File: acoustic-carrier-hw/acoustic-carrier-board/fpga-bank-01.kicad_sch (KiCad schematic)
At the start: 11 parts, among them IC1 ECP5-BGA256, Y401 Crystal Oscillator

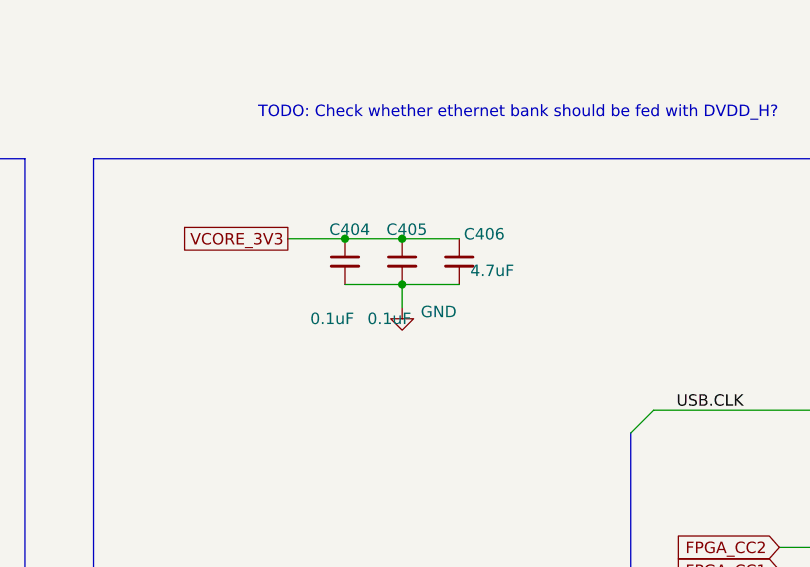
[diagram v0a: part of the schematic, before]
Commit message: [carrier] Added 2 buttons and 2 leds + routing
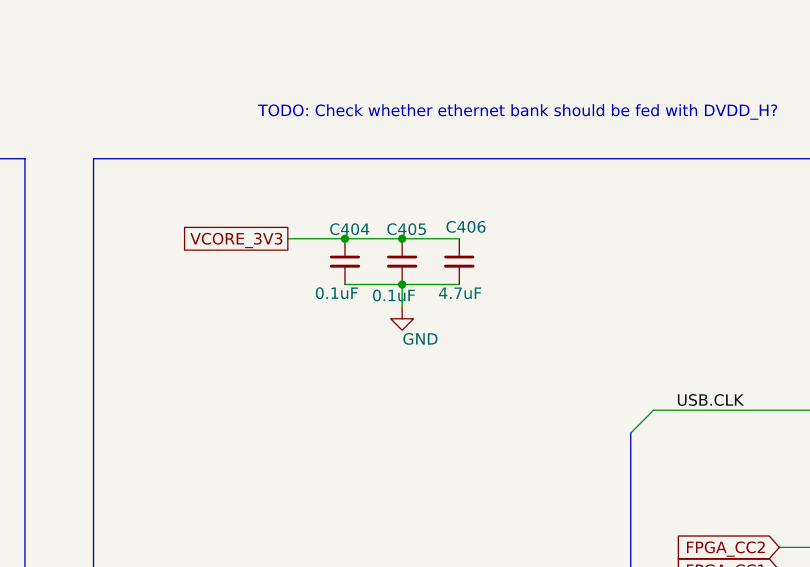
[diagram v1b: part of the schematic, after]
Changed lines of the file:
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@@
 		(dnp no)
 		(property "Reference" "C406"
-			(at 197.358 45.212 0)
+			(at 195.326 44.45 0)
 			(effects
 				(font
@@
 		)
 		(property "Value" "4.7uF"
-			(at 202.946 49.276 0)
+			(at 199.39 51.816 0)
 			(effects
 				(font
@@
 		)
 		(property "Value" "GND"
-			(at 194.564 53.848 0)
+			(at 192.532 56.896 0)
 			(effects
 				(font
@@
 		)
 		(property "Value" "0.1uF"
-			(at 185.166 54.61 0)
+			(at 185.674 51.816 0)
 			(effects
 				(font
@@
 		)
 		(property "Value" "0.1uF"
-			(at 191.516 54.61 0)
+			(at 192.024 52.07 0)
 			(effects
 				(font

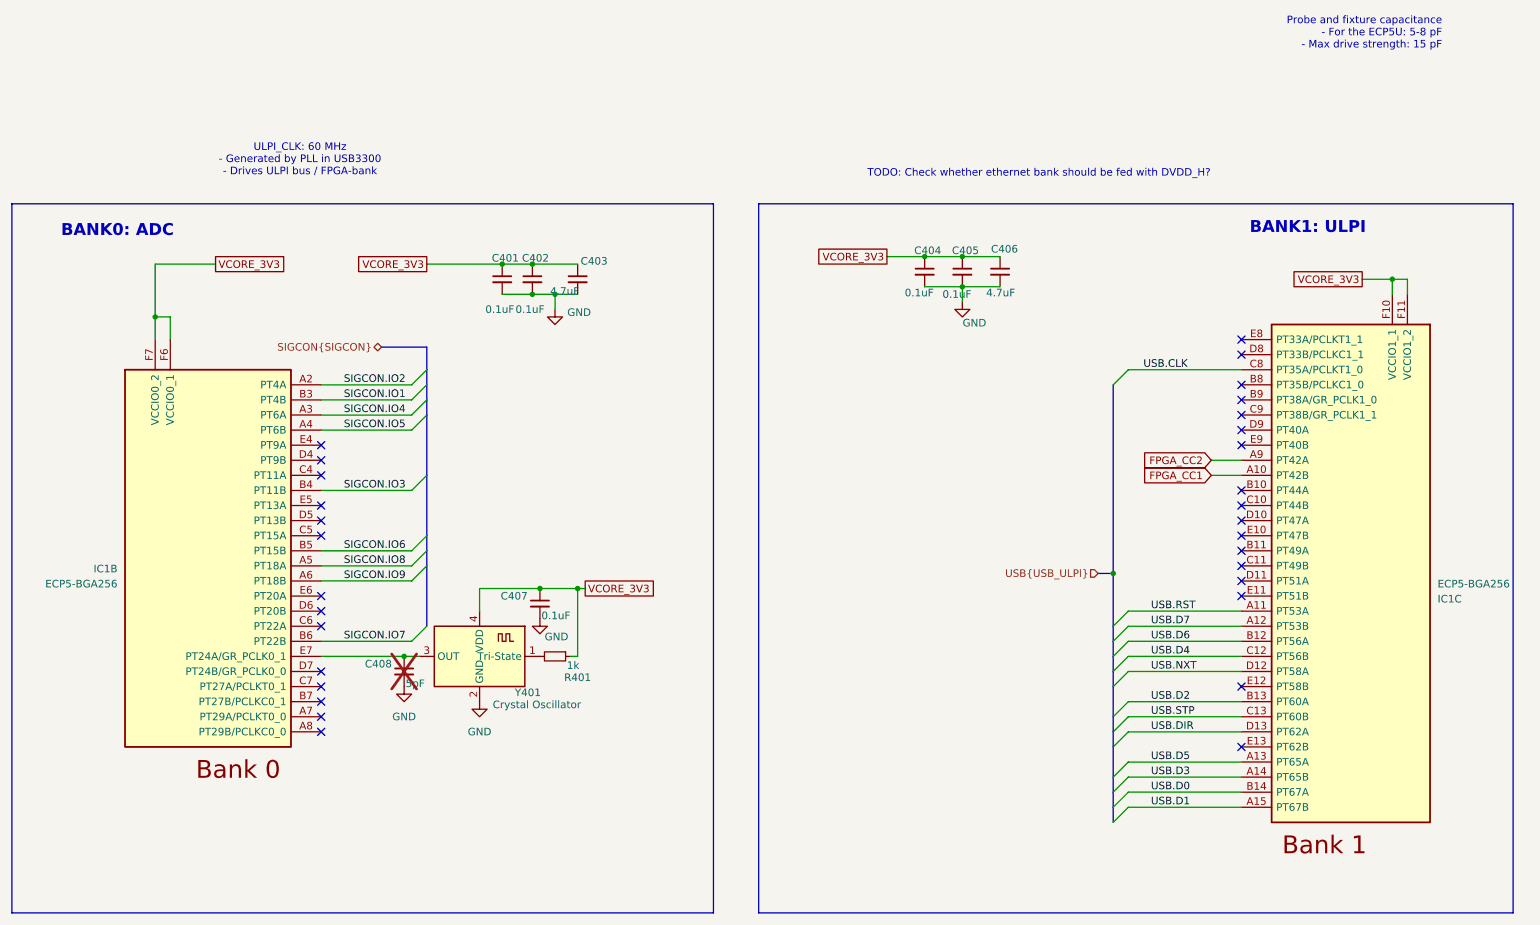
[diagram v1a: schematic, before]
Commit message: [carrier] Added decoupling to LPDDR3 and routed VREF (next) finalize power supply
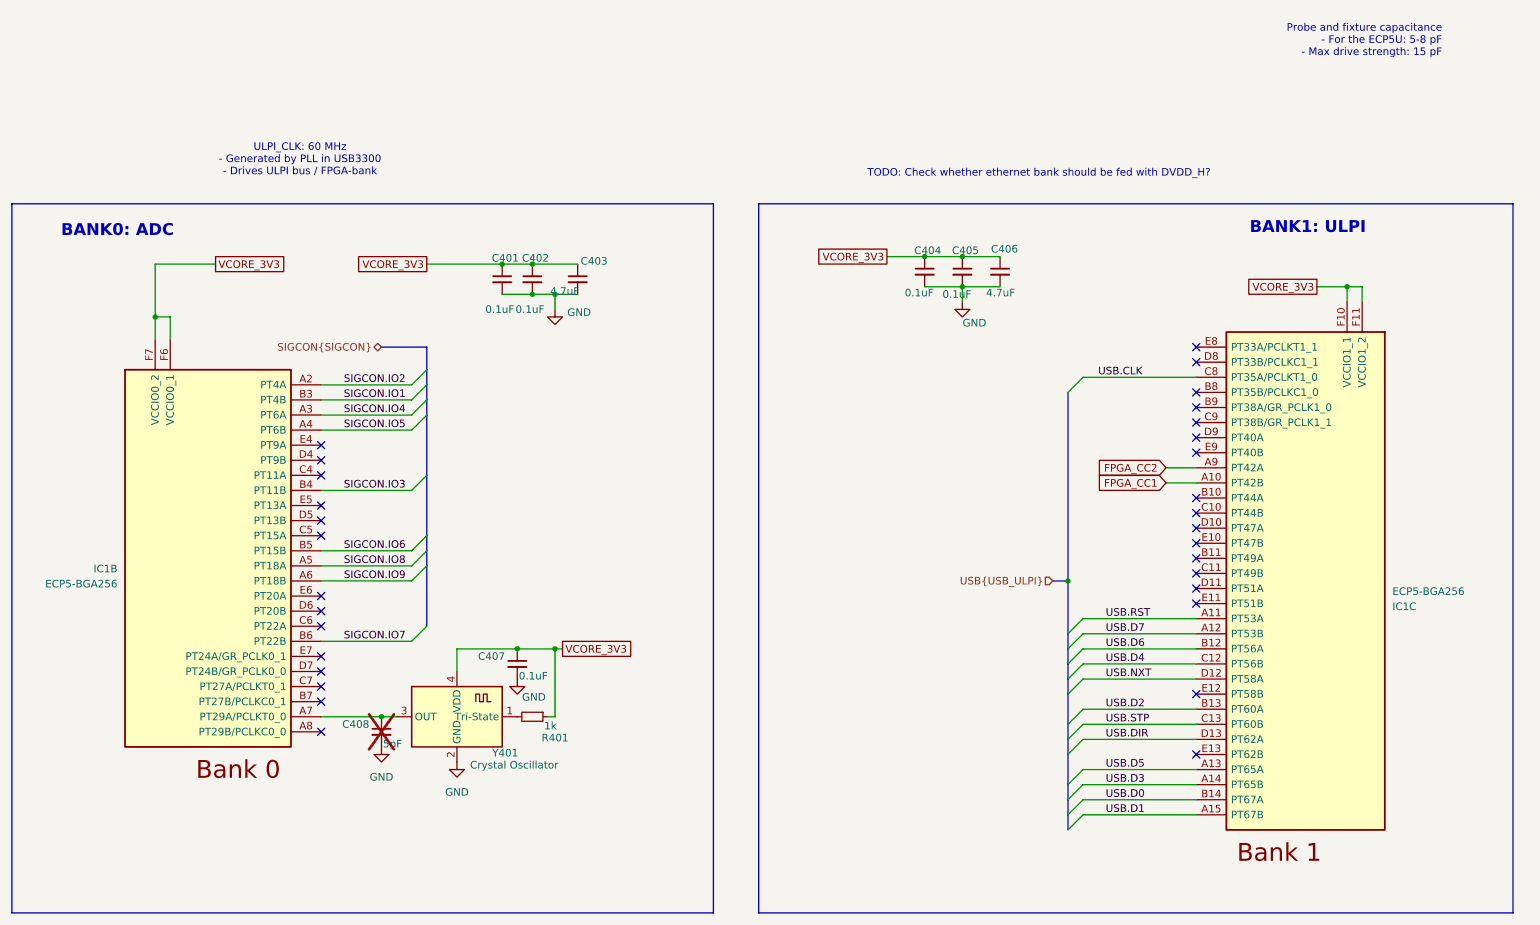
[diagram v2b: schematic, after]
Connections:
- net at C408.1, Y401.3 (OUT): now also IC1.A7 (PT29A/PCLKT0_0); no longer IC1.E7 (PT24A/GR_PCLK0_1)
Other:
- moved on the sheet: C407, C408, IC1C, R401, Y401

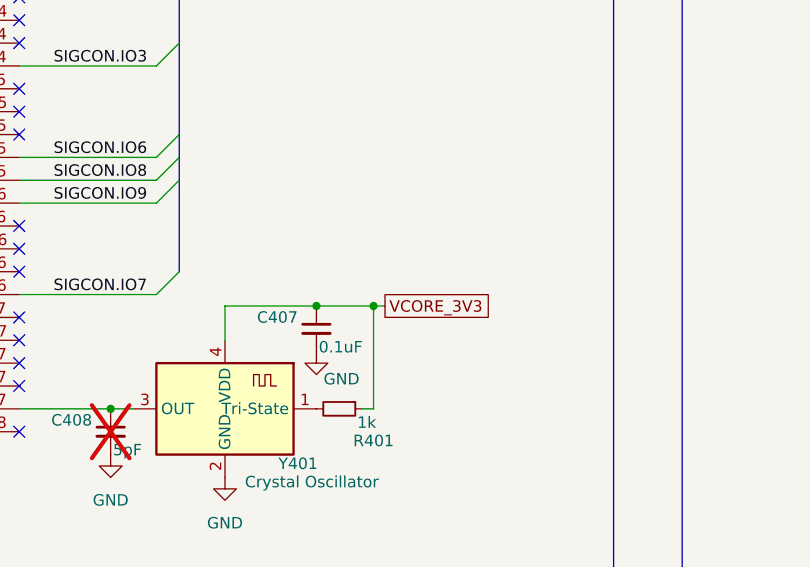
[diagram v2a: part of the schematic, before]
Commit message: [carrier] added silkscreen, moved lpddr3 traces around slightly
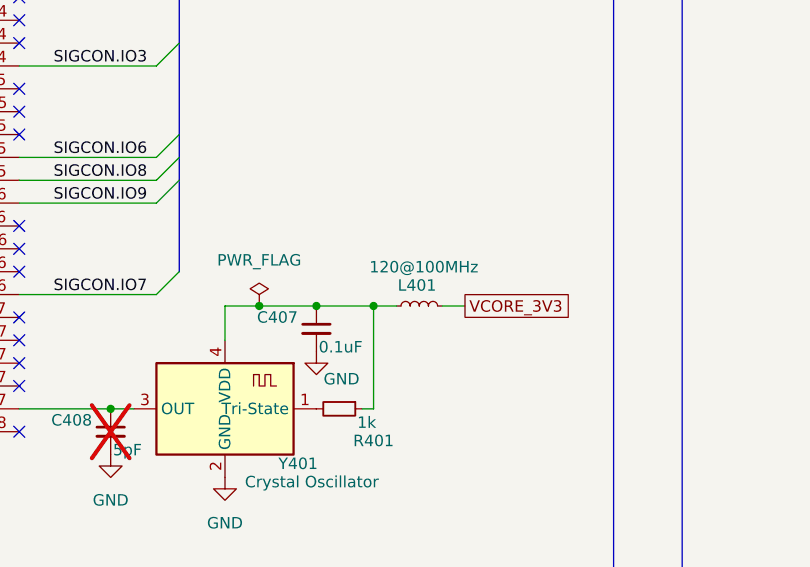
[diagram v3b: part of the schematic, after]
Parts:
- added L401: 120@100MHz, Inductor_SMD:L_0603_1608Metric, symbol Device:L_Small
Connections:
- net VCORE_3V3: now also L401.1; no longer C407.1, R401.1, Y401.4 (VDD)
- new net: C407.1, L401.2, R401.1, Y401.4 (VDD)

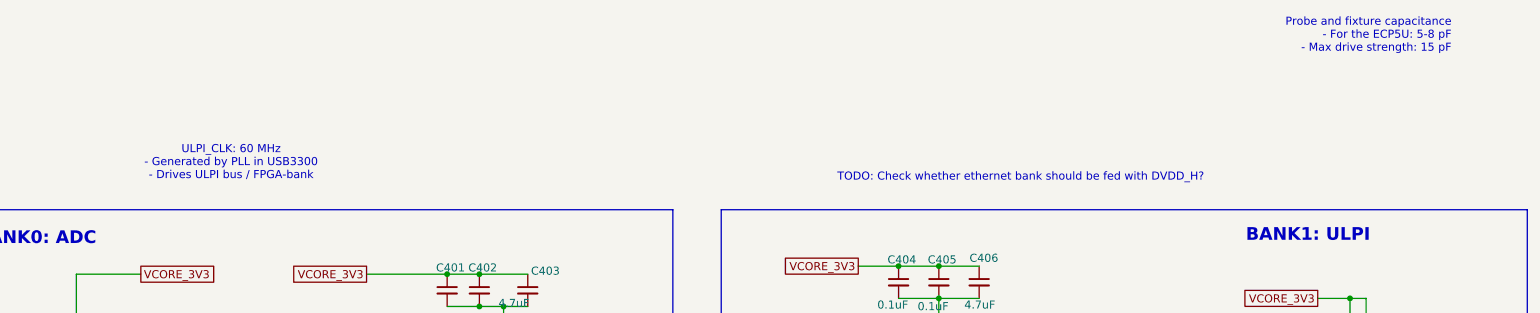
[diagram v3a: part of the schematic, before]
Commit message: [carrier] finished final review, (next) posting to linkedin, start working on analog front-end board
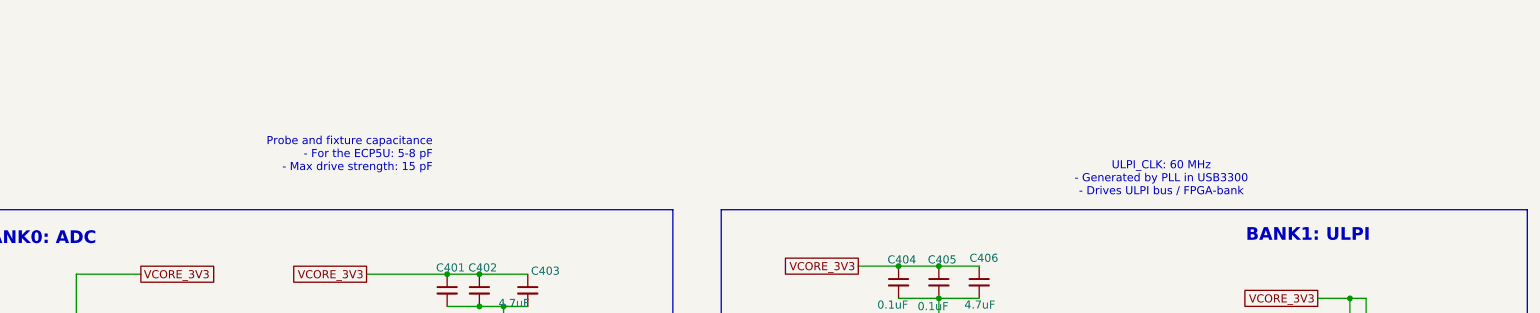
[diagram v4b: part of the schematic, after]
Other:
- note removed: "TODO: Check whether ethernet bank should be fed with DVDD_H?"
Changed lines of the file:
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@@
 	(text "Probe and fixture capacitance\n- For the ECP5U: 5-8 pF\n- Max drive strength: 15 pF"
 		(exclude_from_sim no)
-		(at 271.272 9.398 0)
+		(at 110.744 28.194 0)
 		(effects
 			(font
@@
 		)
 	)
-	(text "TODO: Check whether ethernet bank should be fed with DVDD_H?"
-		(exclude_from_sim no)
-		(at 174.498 31.75 0)
-		(effects
-			(font
-				(size 1.27 1.27)
-			)
-			(justify left)
-		)
-	)
 	(text "BANK0: ADC"
 		(exclude_from_sim no)
@@
 	(text "ULPI_CLK: 60 MHz\n- Generated by PLL in USB3300\n- Drives ULPI bus / FPGA-bank"
 		(exclude_from_sim no)
-		(at 78.994 29.464 0)
+		(at 225.552 32.004 0)
 		(effects
 			(font
